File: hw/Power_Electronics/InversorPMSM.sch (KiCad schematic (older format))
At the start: 114 parts, among them J1 FROM_CONTROL_BOARD, J2 MEASURE_CONN, Q1 HY1908D, Q10 JCS24N50WH, Q11 JCS24N50WH, Q12 JCS24N50WH, Q2 HY1908D, Q3 HY1908D, Q4 HY1908D, Q5 HY1908D, Q6 HY1908D, Q7 JCS24N50WH, Q8 JCS24N50WH, Q9 JCS24N50WH, U1 STDRIVE601

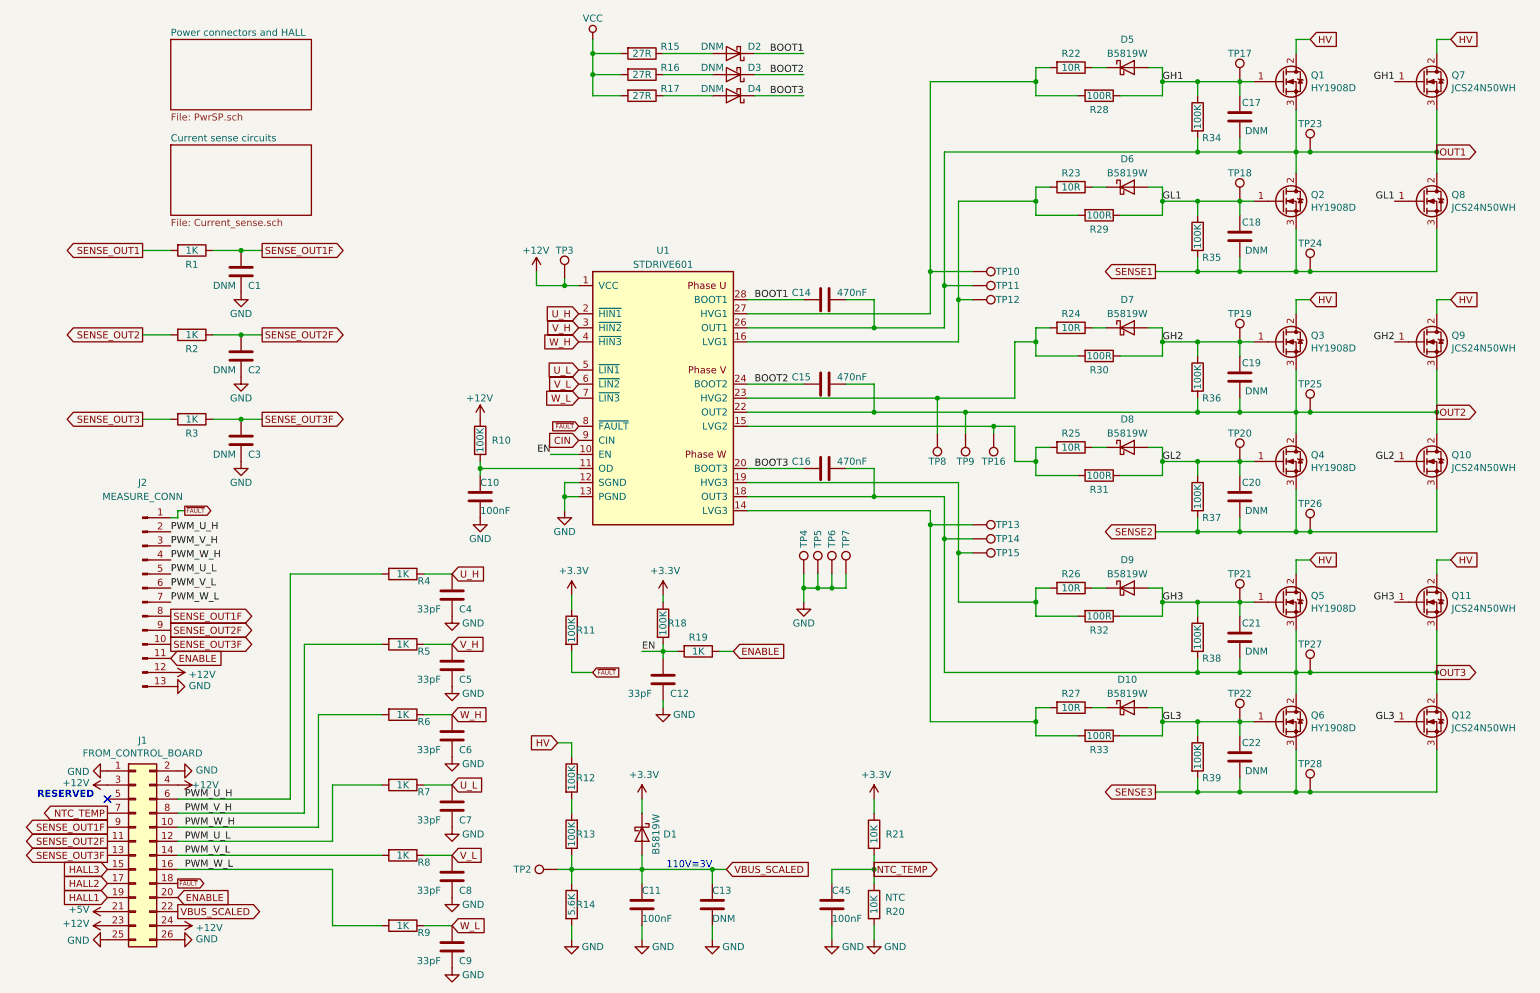
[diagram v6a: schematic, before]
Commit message: create high voltage net class and solve DRC erros
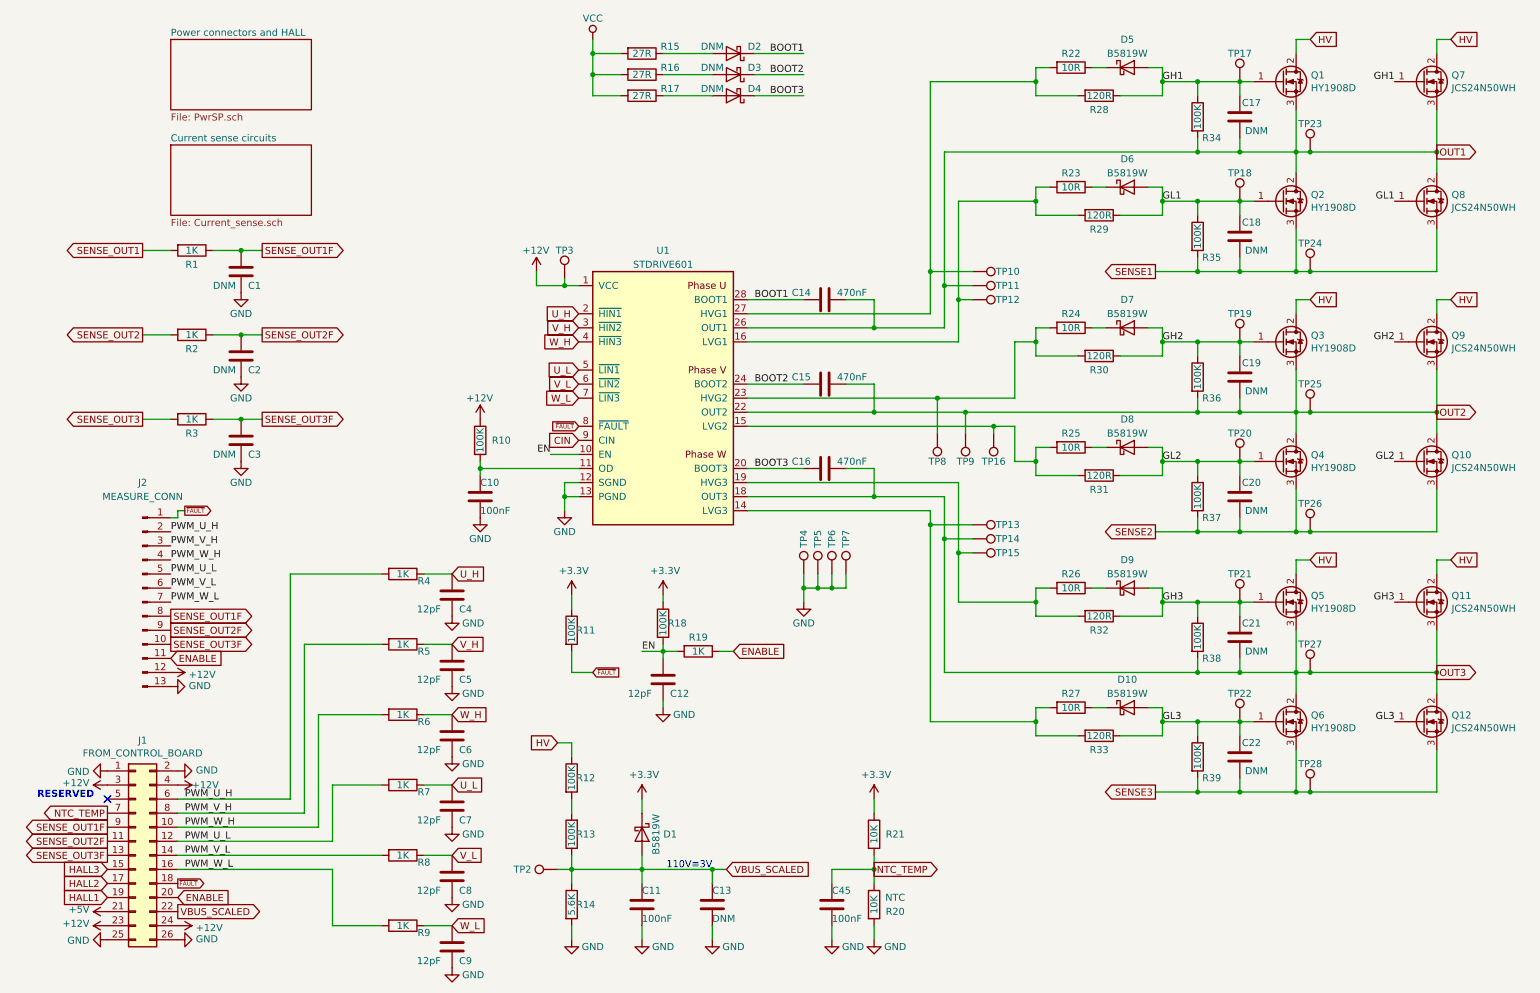
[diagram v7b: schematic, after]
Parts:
- C12, C4, C5, C6, C7, C8, C9: value 33pF -> 12pF; LCSC C1663 -> C38523
- R28, R29, R30, R31, R32, R33: value 100R -> 120R; LCSC C22775 -> C17437
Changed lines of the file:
@@
 P 8100 1400
 F 0 "R28" V 8200 1400 50  0000 C CNN
-F 1 "100R" V 8100 1400 50  0000 C CNN
+F 1 "120R" V 8100 1400 50  0000 C CNN
 F 2 "Resistor_SMD:R_0603_1608Metric" V 8030 1400 50  0001 C CNN
 F 3 "Uniroyal-Elec-0603WAF1000T5E_C22775.pdf" H 8100 1400 50  0001 C CNN
-F 4 "C22775" V 8100 1400 50  0001 C CNN "LCSC"
+F 4 "C17437" V 8100 1400 50  0001 C CNN "LCSC"
 	1    8100 1400
 	0    1    1    0
@@
 P 8100 2250
 F 0 "R29" V 8200 2250 50  0000 C CNN
-F 1 "100R" V 8100 2250 50  0000 C CNN
+F 1 "120R" V 8100 2250 50  0000 C CNN
 F 2 "Resistor_SMD:R_0603_1608Metric" V 8030 2250 50  0001 C CNN
 F 3 "Uniroyal-Elec-0603WAF1000T5E_C22775.pdf" H 8100 2250 50  0001 C CNN
-F 4 "C22775" V 8100 2250 50  0001 C CNN "LCSC"
+F 4 "C17437" V 8100 2250 50  0001 C CNN "LCSC"
 	1    8100 2250
 	0    1    1    0
@@
 P 8100 3250
 F 0 "R30" V 8200 3250 50  0000 C CNN
-F 1 "100R" V 8100 3250 50  0000 C CNN
+F 1 "120R" V 8100 3250 50  0000 C CNN
 F 2 "Resistor_SMD:R_0603_1608Metric" V 8030 3250 50  0001 C CNN
 F 3 "Uniroyal-Elec-0603WAF1000T5E_C22775.pdf" H 8100 3250 50  0001 C CNN
-F 4 "C22775" V 8100 3250 50  0001 C CNN "LCSC"
+F 4 "C17437" V 8100 3250 50  0001 C CNN "LCSC"
 	1    8100 3250
 	0    1    1    0
@@
 P 8100 4100
 F 0 "R31" V 8200 4100 50  0000 C CNN
-F 1 "100R" V 8100 4100 50  0000 C CNN
+F 1 "120R" V 8100 4100 50  0000 C CNN
 F 2 "Resistor_SMD:R_0603_1608Metric" V 8030 4100 50  0001 C CNN
 F 3 "Uniroyal-Elec-0603WAF1000T5E_C22775.pdf" H 8100 4100 50  0001 C CNN
-F 4 "C22775" V 8100 4100 50  0001 C CNN "LCSC"
+F 4 "C17437" V 8100 4100 50  0001 C CNN "LCSC"
 	1    8100 4100
 	0    1    1    0
@@
 P 8100 5100
 F 0 "R32" V 8200 5100 50  0000 C CNN
-F 1 "100R" V 8100 5100 50  0000 C CNN
+F 1 "120R" V 8100 5100 50  0000 C CNN
 F 2 "Resistor_SMD:R_0603_1608Metric" V 8030 5100 50  0001 C CNN
 F 3 "Uniroyal-Elec-0603WAF1000T5E_C22775.pdf" H 8100 5100 50  0001 C CNN
-F 4 "C22775" V 8100 5100 50  0001 C CNN "LCSC"
+F 4 "C17437" V 8100 5100 50  0001 C CNN "LCSC"
 	1    8100 5100
 	0    1    1    0
@@
 P 8100 5950
 F 0 "R33" V 8200 5950 50  0000 C CNN
-F 1 "100R" V 8100 5950 50  0000 C CNN
+F 1 "120R" V 8100 5950 50  0000 C CNN
 F 2 "Resistor_SMD:R_0603_1608Metric" V 8030 5950 50  0001 C CNN
 F 3 "Uniroyal-Elec-0603WAF1000T5E_C22775.pdf" H 8100 5950 50  0001 C CNN
-F 4 "C22775" V 8100 5950 50  0001 C CNN "LCSC"
+F 4 "C17437" V 8100 5950 50  0001 C CNN "LCSC"
 	1    8100 5950
 	0    1    1    0
@@
 P 3500 7450
 F 0 "C9" H 3550 7350 50  0000 L CNN
-F 1 "33pF" H 3250 7350 50  0000 L CNN
+F 1 "12pF" H 3250 7350 50  0000 L CNN
 F 2 "Capacitor_SMD:C_0603_1608Metric" H 3538 7300 50  0001 C CNN
 F 3 "Samsung-Electro-Mechanics-CL10C330JB8NNNC_C1663.pdf" H 3500 7450 50  0001 C CNN
-F 4 "C1663" H 3500 7450 50  0001 C CNN "LCSC"
+F 4 "C38523" H 3500 7450 50  0001 C CNN "LCSC"
 	1    3500 7450
 	1    0    0    -1
@@
 P 3500 6950
 F 0 "C8" H 3550 6850 50  0000 L CNN
-F 1 "33pF" H 3250 6850 50  0000 L CNN
+F 1 "12pF" H 3250 6850 50  0000 L CNN
 F 2 "Capacitor_SMD:C_0603_1608Metric" H 3538 6800 50  0001 C CNN
 F 3 "Samsung-Electro-Mechanics-CL10C330JB8NNNC_C1663.pdf" H 3500 6950 50  0001 C CNN
-F 4 "C1663" H 3500 6950 50  0001 C CNN "LCSC"
+F 4 "C38523" H 3500 6950 50  0001 C CNN "LCSC"
 	1    3500 6950
 	1    0    0    -1
@@
 P 3500 6450
 F 0 "C7" H 3550 6350 50  0000 L CNN
-F 1 "33pF" H 3250 6350 50  0000 L CNN
+F 1 "12pF" H 3250 6350 50  0000 L CNN
 F 2 "Capacitor_SMD:C_0603_1608Metric" H 3538 6300 50  0001 C CNN
 F 3 "Samsung-Electro-Mechanics-CL10C330JB8NNNC_C1663.pdf" H 3500 6450 50  0001 C CNN
-F 4 "C1663" H 3500 6450 50  0001 C CNN "LCSC"
+F 4 "C38523" H 3500 6450 50  0001 C CNN "LCSC"
 	1    3500 6450
 	1    0    0    -1
@@
 P 3500 5950
 F 0 "C6" H 3550 5850 50  0000 L CNN
-F 1 "33pF" H 3250 5850 50  0000 L CNN
+F 1 "12pF" H 3250 5850 50  0000 L CNN
 F 2 "Capacitor_SMD:C_0603_1608Metric" H 3538 5800 50  0001 C CNN
 F 3 "Samsung-Electro-Mechanics-CL10C330JB8NNNC_C1663.pdf" H 3500 5950 50  0001 C CNN
-F 4 "C1663" H 3500 5950 50  0001 C CNN "LCSC"
+F 4 "C38523" H 3500 5950 50  0001 C CNN "LCSC"
 	1    3500 5950
 	1    0    0    -1
@@
 P 3500 5450
 F 0 "C5" H 3550 5350 50  0000 L CNN
-F 1 "33pF" H 3250 5350 50  0000 L CNN
+F 1 "12pF" H 3250 5350 50  0000 L CNN
 F 2 "Capacitor_SMD:C_0603_1608Metric" H 3538 5300 50  0001 C CNN
 F 3 "Samsung-Electro-Mechanics-CL10C330JB8NNNC_C1663.pdf" H 3500 5450 50  0001 C CNN
-F 4 "C1663" H 3500 5450 50  0001 C CNN "LCSC"
+F 4 "C38523" H 3500 5450 50  0001 C CNN "LCSC"
 	1    3500 5450
 	1    0    0    -1
@@
 P 3500 4950
 F 0 "C4" H 3550 4850 50  0000 L CNN
-F 1 "33pF" H 3250 4850 50  0000 L CNN
+F 1 "12pF" H 3250 4850 50  0000 L CNN
 F 2 "Capacitor_SMD:C_0603_1608Metric" H 3538 4800 50  0001 C CNN
 F 3 "Samsung-Electro-Mechanics-CL10C330JB8NNNC_C1663.pdf" H 3500 4950 50  0001 C CNN
-F 4 "C1663" H 3500 4950 50  0001 C CNN "LCSC"
+F 4 "C38523" H 3500 4950 50  0001 C CNN "LCSC"
 	1    3500 4950
 	1    0    0    -1
@@
 P 5000 5550
 F 0 "C12" H 5050 5450 50  0000 L CNN
-F 1 "33pF" H 4750 5450 50  0000 L CNN
+F 1 "12pF" H 4750 5450 50  0000 L CNN
 F 2 "Capacitor_SMD:C_0603_1608Metric" H 5038 5400 50  0001 C CNN
 F 3 "Samsung-Electro-Mechanics-CL10C330JB8NNNC_C1663.pdf" H 5000 5550 50  0001 C CNN
-F 4 "C1663" H 5000 5550 50  0001 C CNN "LCSC"
+F 4 "C38523" H 5000 5550 50  0001 C CNN "LCSC"
 	1    5000 5550
 	1    0    0    -1
